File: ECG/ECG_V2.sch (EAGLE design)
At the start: 32 parts, among them J1 TC2030-CTX-NL, U1 AD8232, U4 BGM111-VISUAL-A

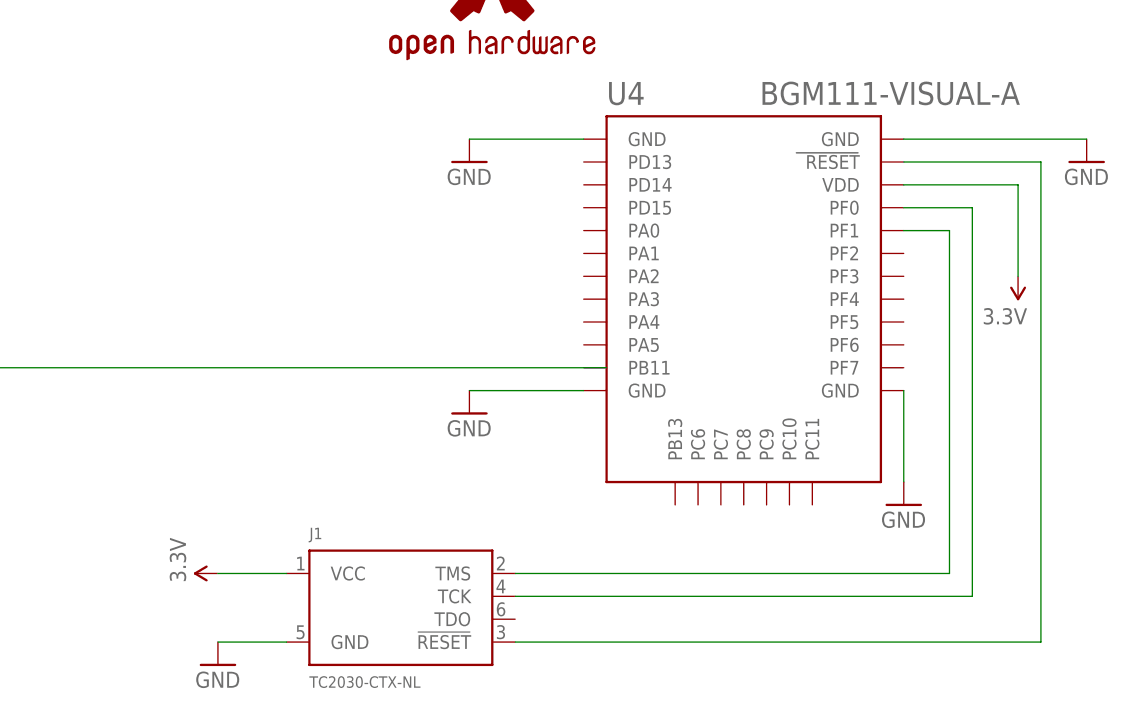
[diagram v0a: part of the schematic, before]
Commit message: Added new tag connect component and corrected pin configuation
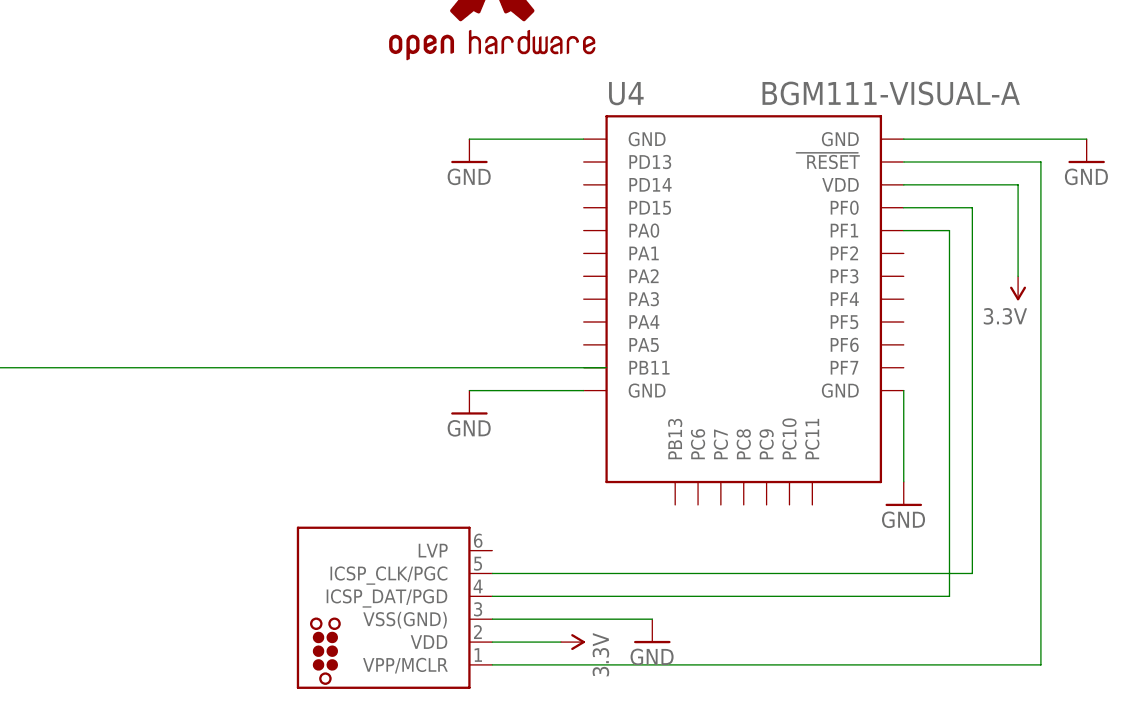
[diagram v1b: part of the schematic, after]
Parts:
- J1: value TC2030-CTX-NL -> (none); device tag_connector:TC2030-CTX-NL -> tag-connect:TC2030-MCP-NL
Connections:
- removed net N$36: J1.TMS, U4.PF1
- removed net N$37: J1.TCK, U4.PF0
- new net N$2: J1.ICSP_CLK/PGC, U4.PF0
- new net N$6: J1.ICSP_DAT/PGD, U4.PF1
- net 3.3V: no longer J1.VCC
- net GND: now also J1.VSS(GND); no longer J1.GND
- net N$38: now also J1.VPP/MCLR; no longer J1.!RESET
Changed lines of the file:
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@@
 <part name="SUPPLY11" library="SparkFun-Aesthetics" deviceset="3.3V" device=""/>
 <part name="GND14" library="SparkFun-Aesthetics" deviceset="GND" device=""/>
-<part name="J1" library="tag_connector" deviceset="TC2030-CTX" device="-NL"/>
 <part name="SUPPLY12" library="SparkFun-Aesthetics" deviceset="3.3V" device=""/>
 <part name="GND15" library="SparkFun-Aesthetics" deviceset="GND" device=""/>
@@
 <part name="JP2" library="LilyPad-Wearables" deviceset="SEWTAP" device="2"/>
 <part name="BAT2" library="SMTU-2032-1" deviceset="2032" device=""/>
+<part name="J1" library="tag-connect" deviceset="TC2030" device="-MCP-NL"/>
 </parts>
 <sheets>
@@
 <instance part="GND13" gate="1" x="215.9" y="-60.96"/>
 <instance part="SUPPLY11" gate="G$1" x="208.28" y="-73.66" rot="R180"/>
-<instance part="GND14" gate="1" x="119.38" y="-116.84"/>
-<instance part="J1" gate="G$1" x="139.7" y="-109.22"/>
-<instance part="SUPPLY12" gate="G$1" x="119.38" y="-106.68" rot="R90"/>
+<instance part="GND14" gate="1" x="167.64" y="-114.3"/>
+<instance part="SUPPLY12" gate="G$1" x="157.48" y="-114.3" rot="R270"/>
 <instance part="GND15" gate="1" x="25.4" y="-45.72" smashed="yes">
 <attribute name="VALUE" x="22.86" y="-48.26" size="1.778" layer="96"/>
@@
 <instance part="JP2" gate="G$1" x="43.18" y="30.48" rot="R180"/>
 <instance part="BAT2" gate="G$1" x="17.78" y="-43.18" rot="R180"/>
+<instance part="J1" gate="G$1" x="137.16" y="-109.22" rot="R180"/>
 </instances>
 <busses>
@@
 </segment>
 <segment>
-<pinref part="GND14" gate="1" pin="GND"/>
-<pinref part="J1" gate="G$1" pin="GND"/>
-<wire x1="119.38" y1="-114.3" x2="127" y2="-114.3" width="0.1524" layer="91"/>
-</segment>
-<segment>
 <pinref part="GND15" gate="1" pin="GND"/>
 <wire x1="22.86" y1="-43.18" x2="25.4" y2="-43.18" width="0.1524" layer="91"/>
 <pinref part="BAT2" gate="G$1" pin="-"/>
+</segment>
+<segment>
+<pinref part="J1" gate="G$1" pin="VSS(GND)"/>
+<pinref part="GND14" gate="1" pin="GND"/>
+<wire x1="149.86" y1="-111.76" x2="167.64" y2="-111.76" width="0.1524" layer="91"/>
 </segment>
 </net>
@@
 <segment>
 <pinref part="SUPPLY12" gate="G$1" pin="3.3V"/>
-<pinref part="J1" gate="G$1" pin="VCC"/>
-<wire x1="119.38" y1="-106.68" x2="127" y2="-106.68" width="0.1524" layer="91"/>
+<wire x1="157.48" y1="-114.3" x2="149.86" y2="-114.3" width="0.1524" layer="91"/>
 </segment>
 <segment>
@@
 </segment>
 </net>
-<net name="N$36" class="0">
+<net name="N$38" class="0">
+<segment>
+<wire x1="149.86" y1="-116.84" x2="210.82" y2="-116.84" width="0.1524" layer="91"/>
+<wire x1="210.82" y1="-116.84" x2="210.82" y2="-60.96" width="0.1524" layer="91"/>
+<wire x1="210.82" y1="-60.96" x2="195.58" y2="-60.96" width="0.1524" layer="91"/>
+<pinref part="U4" gate="G$1" pin="RESET"/>
+<pinref part="J1" gate="G$1" pin="VPP/MCLR"/>
+</segment>
+</net>
+<net name="N$2" class="0">
+<segment>
+<pinref part="U4" gate="G$1" pin="PF0"/>
+<wire x1="195.58" y1="-66.04" x2="203.2" y2="-66.04" width="0.1524" layer="91"/>
+<pinref part="J1" gate="G$1" pin="ICSP_CLK/PGC"/>
+<wire x1="149.86" y1="-106.68" x2="203.2" y2="-106.68" width="0.1524" layer="91"/>
+<wire x1="203.2" y1="-106.68" x2="203.2" y2="-66.04" width="0.1524" layer="91"/>
+</segment>
+</net>
+<net name="N$6" class="0">
 <segment>
 <pinref part="U4" gate="G$1" pin="PF1"/>
 <wire x1="195.58" y1="-68.58" x2="200.66" y2="-68.58" width="0.1524" layer="91"/>
-<pinref part="J1" gate="G$1" pin="TMS"/>
-<wire x1="152.4" y1="-106.68" x2="200.66" y2="-106.68" width="0.1524" layer="91"/>
-<wire x1="200.66" y1="-106.68" x2="200.66" y2="-68.58" width="0.1524" layer="91"/>
-</segment>
-</net>
-<net name="N$37" class="0">
-<segment>
-<pinref part="U4" gate="G$1" pin="PF0"/>
-<wire x1="195.58" y1="-66.04" x2="203.2" y2="-66.04" width="0.1524" layer="91"/>
-<wire x1="203.2" y1="-66.04" x2="203.2" y2="-109.22" width="0.1524" layer="91"/>
-<pinref part="J1" gate="G$1" pin="TCK"/>
-<wire x1="203.2" y1="-109.22" x2="152.4" y2="-109.22" width="0.1524" layer="91"/>
-</segment>
-</net>
-<net name="N$38" class="0">
-<segment>
-<wire x1="152.4" y1="-114.3" x2="210.82" y2="-114.3" width="0.1524" layer="91"/>
-<wire x1="210.82" y1="-114.3" x2="210.82" y2="-60.96" width="0.1524" layer="91"/>
-<wire x1="210.82" y1="-60.96" x2="195.58" y2="-60.96" width="0.1524" layer="91"/>
-<pinref part="U4" gate="G$1" pin="RESET"/>
-<pinref part="J1" gate="G$1" pin="!RESET"/>
-</segment>
-</net>
+<wire x1="200.66" y1="-68.58" x2="200.66" y2="-109.22" width="0.1524" layer="91"/>
+<pinref part="J1" gate="G$1" pin="ICSP_DAT/PGD"/>
+<wire x1="200.66" y1="-109.22" x2="149.86" y2="-109.22" width="0.1524" layer="91"/>
+</segment>
+</net>

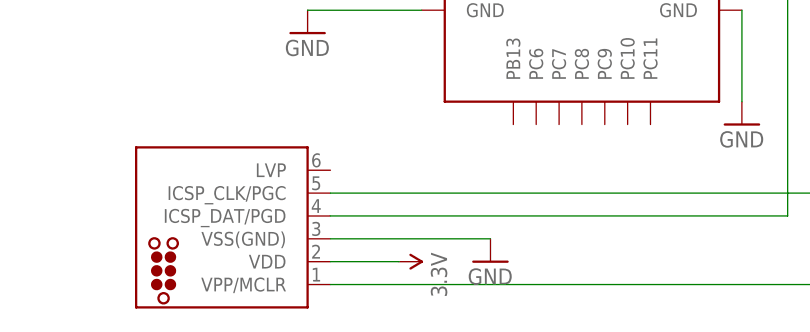
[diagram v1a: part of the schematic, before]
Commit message: Corrected the Supply issue with tag connect and changed width of some routes
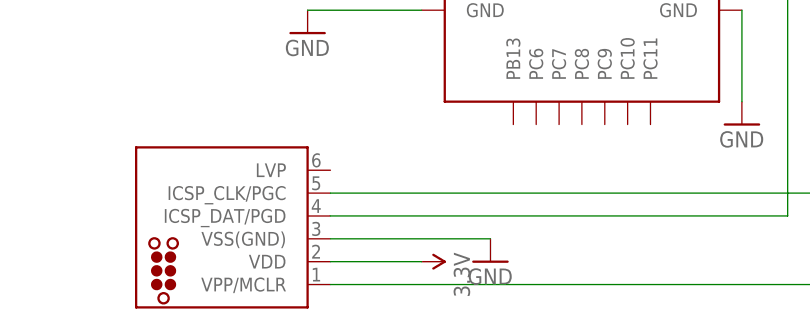
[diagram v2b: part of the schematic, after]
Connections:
- net 3.3V: now also J1.VDD
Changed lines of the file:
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@@
 <part name="SUPPLY11" library="SparkFun-Aesthetics" deviceset="3.3V" device=""/>
 <part name="GND14" library="SparkFun-Aesthetics" deviceset="GND" device=""/>
-<part name="SUPPLY12" library="SparkFun-Aesthetics" deviceset="3.3V" device=""/>
 <part name="GND15" library="SparkFun-Aesthetics" deviceset="GND" device=""/>
 <part name="SUPPLY13" library="SparkFun-Aesthetics" deviceset="3.3V" device=""/>
@@
 <part name="BAT2" library="SMTU-2032-1" deviceset="2032" device=""/>
 <part name="J1" library="tag-connect" deviceset="TC2030" device="-MCP-NL"/>
+<part name="SUPPLY1" library="SparkFun-Aesthetics" deviceset="3.3V" device=""/>
 </parts>
 <sheets>
@@
 <instance part="SUPPLY11" gate="G$1" x="208.28" y="-73.66" rot="R180"/>
 <instance part="GND14" gate="1" x="167.64" y="-114.3"/>
-<instance part="SUPPLY12" gate="G$1" x="157.48" y="-114.3" rot="R270"/>
 <instance part="GND15" gate="1" x="25.4" y="-45.72" smashed="yes">
 <attribute name="VALUE" x="22.86" y="-48.26" size="1.778" layer="96"/>
@@
 <instance part="BAT2" gate="G$1" x="17.78" y="-43.18" rot="R180"/>
 <instance part="J1" gate="G$1" x="137.16" y="-109.22" rot="R180"/>
+<instance part="SUPPLY1" gate="G$1" x="160.02" y="-114.3" rot="R270"/>
 </instances>
 <busses>
@@
 </segment>
 <segment>
-<pinref part="SUPPLY12" gate="G$1" pin="3.3V"/>
-<wire x1="157.48" y1="-114.3" x2="149.86" y2="-114.3" width="0.1524" layer="91"/>
-</segment>
-<segment>
 <pinref part="U4" gate="G$1" pin="VDD"/>
 <wire x1="195.58" y1="-63.5" x2="208.28" y2="-63.5" width="0.1524" layer="91"/>
@@
 <pinref part="BAT2" gate="G$1" pin="+"/>
 </segment>
-</net>
+<segment>
+<pinref part="J1" gate="G$1" pin="VDD"/>
+<pinref part="SUPPLY1" gate="G$1" pin="3.3V"/>
+<wire x1="149.86" y1="-114.3" x2="160.02" y2="-114.3" width="0.1524" layer="91"/>
+</segment>
+</net>
